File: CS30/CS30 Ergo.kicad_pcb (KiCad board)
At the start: 2 copper layers, 230.5 x 75.4 mm, 63 parts, among them U0 ProMicro

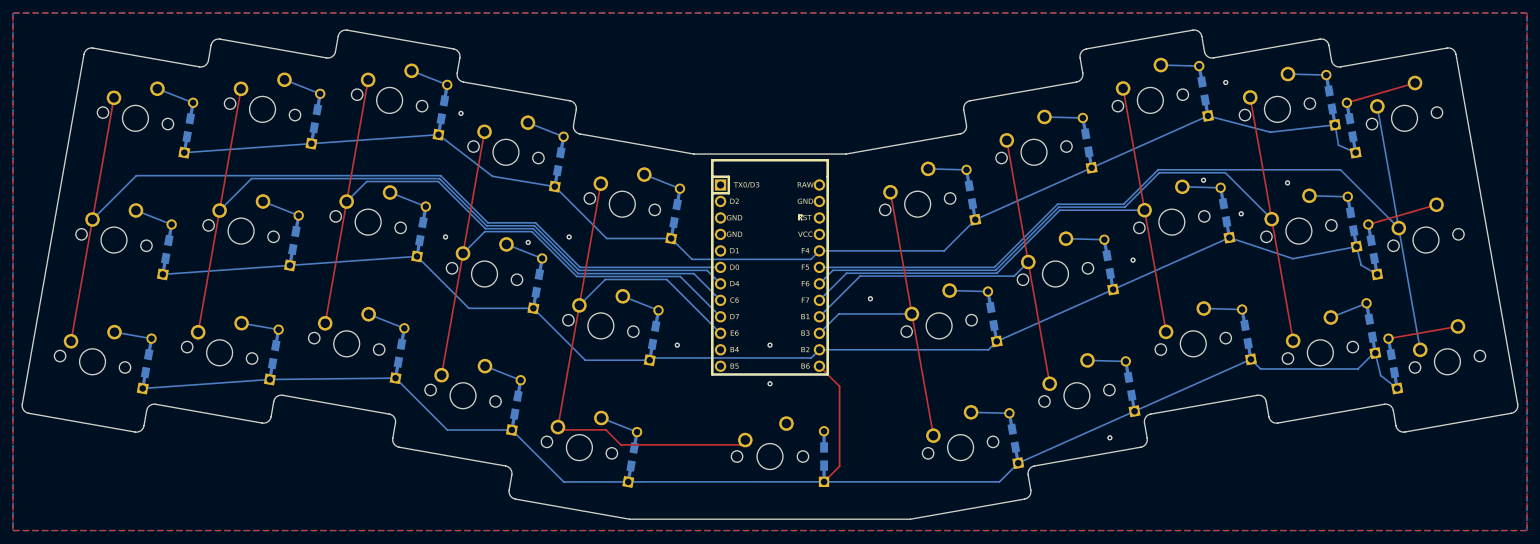
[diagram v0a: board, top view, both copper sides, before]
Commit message: Rerouted Ergo and created test gerbers
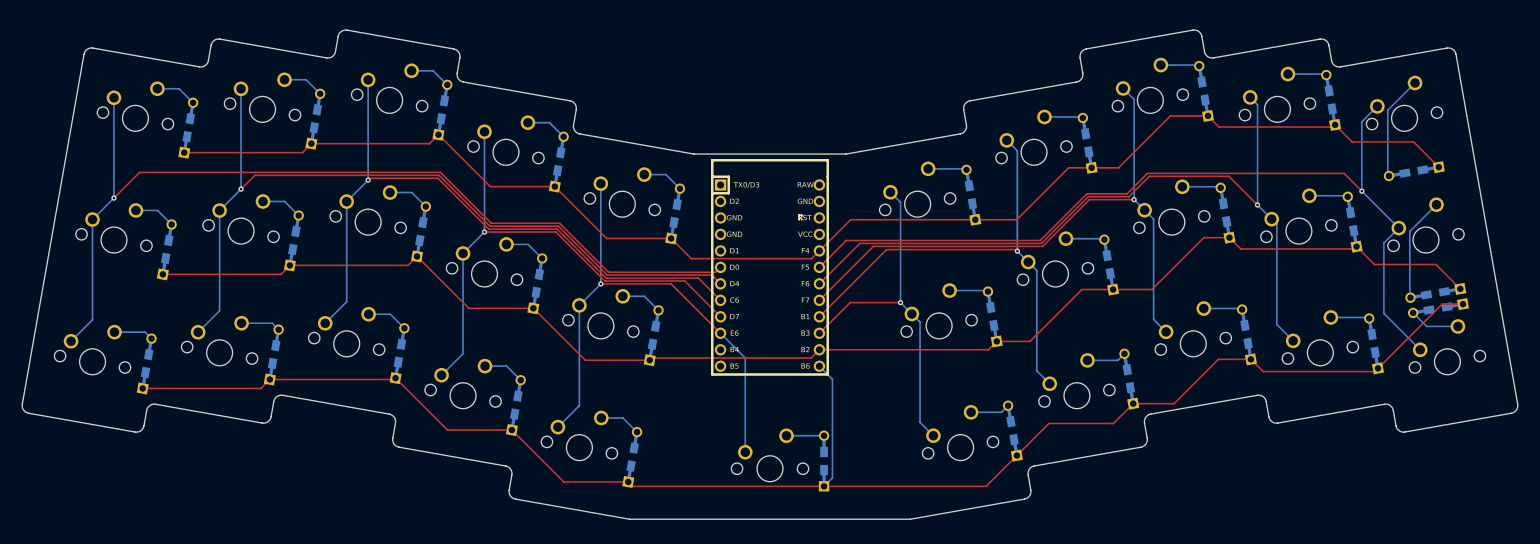
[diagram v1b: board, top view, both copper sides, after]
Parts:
- moved D9 11.8 mm to (242.1, 72.1), turned to 10 degrees
- moved D19 11.8 mm to (245.4, 90.8), turned to 10 degrees
- moved D30 11.0 mm to (245.8, 93.2), turned to 10 degrees
- moved D29 2.38 mm to (235.9, 98.6)
- moved MX25 1.88 mm to (142.9, 117.9)
- moved D26 1.19 mm to (180.3, 112.0)
- moved D27 1.19 mm to (198.2, 104.0)
- moved D25 0.69 mm to (151.2, 116.7)
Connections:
- U0 pad 1: (no net) -> Net-(U0-Pad1)
- U0 pad 11: (no net) -> Net-(U0-Pad11)
- U0 pad 12: (no net) -> Net-(U0-Pad12)
- U0 pad 2: (no net) -> Net-(U0-Pad2)
- U0 pad 21: (no net) -> Net-(U0-Pad21)
- U0 pad 22: (no net) -> Net-(U0-Pad22)
- U0 pad 23: GND -> Net-(U0-Pad23)
- U0 pad 24: (no net) -> Net-(U0-Pad24)
- U0 pad 3: GND -> Net-(U0-Pad3)
- U0 pad 4: GND -> Net-(U0-Pad4)
- U0 pad 5: (no net) -> Net-(U0-Pad5)
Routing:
- net ROW0: track 196.8 -> 215.1 mm
- net ROW1: track 201.8 -> 219.1 mm
- net ROW2: track 229.8 -> 244.1 mm
- net COL4: track 95.3 -> 81.8 mm, vias 0 -> 1
- net Net-(D25-Pad2): track 0.00 -> 5.80 mm
- net Net-(D9-Pad2): track 10.9 -> 16.1 mm
- net Net-(D19-Pad2): track 10.9 -> 16.1 mm
- net Net-(D30-Pad2): track 10.9 -> 7.77 mm
- net COL3: track 84.6 -> 82.1 mm, vias 0 -> 1
- net COL9: track 137.3 -> 134.9 mm, vias 0 -> 1
- net COL1: track 124.1 -> 122.0 mm, vias 0 -> 1
- net COL2: track 104.6 -> 102.5 mm, vias 0 -> 1
- net COL0: track 143.6 -> 142.1 mm, vias 0 -> 1
- net COL8: track 117.9 -> 116.5 mm, vias 0 -> 1
- net COL6: track 73.8 -> 75.2 mm, vias 0 -> 1
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- removed copper zone on B.Cu, net GND
- removed copper zone on F.Cu, net GND
